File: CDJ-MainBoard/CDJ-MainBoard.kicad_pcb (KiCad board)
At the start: 4 copper layers, 304.6 x 160 mm, 160 parts, among them J1 J_FAN_PWM, J10 USB_DJ_STICK (USB3_A), J11 USB_SCREEN (USB3_A), J12 HR911130A, J13 PI HDMI_0 (HDMI_D_1.4 micro), J14 PI HDMI_0 (HDMI_D_1.4 micro), J15 USB_C_Receptacle_USB2.0_16P, J16 J_JOG, J17 J_PLAY, J18 J_ENCODER_BACK, J19 J_TOUCH, J2 PJ-611E 6.35mm jack, J20 J_LOOP, J21 J_MASTER_TEMPO, J22 J_TEMPO, J3 J_RCA_L (white), J4 J_RCA_R (red), J5 PJ-320D 3.5mm jack, J6 J_ISP_ATMEGA, J7 J_I2C, J8 AUX POWER USB_A, J9 USB_C_Receptacle_USB2.0_16P, SW1 DSWB05LHGET, SW2 PWR_BUT_CM5, SW3 SW_MAIN_POWER, SW4 RESET_BTN, U1 Compute_Module_5_Functional, U10 AP2112K-3.3 DIGITAL PSU LDO, U11 AP2112K-3.3 ANALOG AUDIO LDO, U12 CH224K, U13 SY8368AQQC, U14 ATmega32U4-A (Arduino MIDI co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, U2 PCM5122PW, U3 AP2553W6-7, U4 AP2553W6-7, U5 AP2553W6-7, U6 USBLC6-2SC6, U7 USBLC6-2SC6, U8 USBLC6-2SC6, U9 AP2553W6-7, X1 X322516MLB4SI

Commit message: Route the buck and fixed pinout on ethernet and 3D model offsets
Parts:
- removed J22: J_TEMPO, Connector_JST:JST_PH_B5B-PH-K_1x05_P2.00mm_Vertical
- added C60: 10uF, PCM_JLCPCB:C_0805, F.Cu at (19.3, 44.2)
- added C61: 100nF, PCM_JLCPCB:C_0402, F.Cu at (173.0, 97.5)
- added C62: 100nF, PCM_JLCPCB:C_0402, F.Cu at (173.0, 99.3)
- added C63: 100nF, PCM_JLCPCB:C_0402, F.Cu at (173.0, 101.2)
- added R41: 10kΩ, PCM_JLCPCB:R_0402, F.Cu at (85.5, 125.5)
- added R52: 10kΩ, PCM_JLCPCB:R_0402, F.Cu at (134.0, 131.9)
- added R53: 4.7kΩ, PCM_JLCPCB:R_0402, F.Cu at (188.5, 127.9)
- added R54: 4.7kΩ, PCM_JLCPCB:R_0402, F.Cu at (188.5, 129.4)
- added R55: 10kΩ, PCM_JLCPCB:R_0402, F.Cu at (168.5, 140.5)
- added R56: 330Ω, PCM_JLCPCB:R_0402, F.Cu at (168.5, 138.7)
- added R57: 330Ω, PCM_JLCPCB:R_0402, F.Cu at (168.5, 136.8)
- added R58: 330Ω, PCM_JLCPCB:R_0402, F.Cu at (168.5, 135.0)
- added R59: 330Ω, PCM_JLCPCB:R_0402, F.Cu at (168.5, 133.1)
- added R60: 330Ω, PCM_JLCPCB:R_0402, F.Cu at (168.5, 131.3)
- added R61: 330Ω, PCM_JLCPCB:R_0402, F.Cu at (168.5, 129.4)
- added R62: 330Ω, PCM_JLCPCB:R_0402, F.Cu at (188.5, 142.0)
- added R63: 330Ω, PCM_JLCPCB:R_0402, F.Cu at (188.5, 140.1)
- added R64: 330Ω, PCM_JLCPCB:R_0402, F.Cu at (188.5, 138.3)
- added R65: 330Ω, PCM_JLCPCB:R_0402, F.Cu at (188.5, 136.4)
- added R66: 330Ω, PCM_JLCPCB:R_0402, F.Cu at (188.5, 134.6)
- added R67: 330Ω, PCM_JLCPCB:R_0402, F.Cu at (188.5, 132.7)
- added R68: 330Ω, PCM_JLCPCB:R_0402, F.Cu at (188.5, 130.9)
- added TP12: PF7, TestPoint:TestPoint_Pad_2.0x2.0mm, F.Cu at (66.4, 104.5)
- added TP13: PF6, TestPoint:TestPoint_Pad_2.0x2.0mm, F.Cu at (66.4, 108.5)
- added TP14: PF5, TestPoint:TestPoint_Pad_2.0x2.0mm, F.Cu at (70.5, 104.5)
- added TP15: PF4, TestPoint:TestPoint_Pad_2.0x2.0mm, F.Cu at (70.5, 108.5)
- added TP16: PF1, TestPoint:TestPoint_Pad_2.0x2.0mm, F.Cu at (74.5, 104.5)
- added TP18: PC7, TestPoint:TestPoint_Pad_2.0x2.0mm, F.Cu at (74.5, 108.5)
- added TP24: I2C_SDA_ARDUINO, TestPoint:TestPoint_Pad_1.5x1.5mm, F.Cu at (80.5, 104.5)
- added TP25: I2C_SCL_ARDUINO, TestPoint:TestPoint_Pad_1.5x1.5mm, F.Cu at (80.5, 109.5)
- added U16: 74HC4067PW,118, JLC2KiCad_lib-footprints:TSSOP-28_L9.8-W6.6-P0.65-BL, F.Cu at (118.0, 133.0)
- added U17: PCM5122PW, Package_SO:TSSOP-28_4.4x9.7mm_P0.65mm, F.Cu at (160.6, -34.7)
- added U18: MCP23017T-E/SS, JLC2KiCad_lib-footprints:SSOP-28_L10.2-W5.3-P0.65-LS7.8-BL, F.Cu at (141.0, 134.5)
- added U19: MCP23017T-E/SS, JLC2KiCad_lib-footprints:SSOP-28_L10.2-W5.3-P0.65-LS7.8-BL, F.Cu at (178.5, 135.6)
- J12: footprint JLC2KiCad_lib-footprints:RJ45-TH_HR911130A -> JLC2KiCad_lib-footprints:RJ45-TH_HR911105A
- J15: value USB_C_Receptacle_USB2.0_16P -> TYPE-C-31-M-12; footprint JLC2KiCad_lib-footprints:USB-C-SMD_TYPE-C-6PIN-2MD-073 -> JLC2KiCad_lib-footprints:USB-C_SMD-TYPE-C-31-M-12_1
- J16: value J_JOG -> J_JOGWHEEL; footprint Connector_JST:JST_PH_B4B-PH-K_1x04_P2.00mm_Vertical -> Connector_JST:JST_PH_B5B-PH-K_1x05_P2.00mm_Vertical
- J17: value J_PLAY -> J_HOTCUES; footprint Connector_JST:JST_PH_B6B-PH-K_1x06_P2.00mm_Vertical -> Connector_JST:JST_PH_B8B-PH-K_1x08_P2.00mm_Vertical
- J18: value J_ENCODER_BACK -> J_LEFT_CTRLS; footprint Connector_JST:JST_PH_B7B-PH-K_1x07_P2.00mm_Vertical -> Connector_JST:JST_PH_B10B-PH-K_1x10_P2.00mm_Vertical
- J19: value J_TOUCH -> J_RIGHT_CTRLS; footprint Connector_JST:JST_PH_B2B-PH-K_1x02_P2.00mm_Vertical -> Connector_JST:JST_PH_B12B-PH-K_1x12_P2.00mm_Vertical
- J20: value J_LOOP -> J_TOP_LEFT; footprint Connector_JST:JST_PH_B8B-PH-K_1x08_P2.00mm_Vertical -> Connector_JST:JST_PH_B10B-PH-K_1x10_P2.00mm_Vertical
- J21: value J_MASTER_TEMPO -> J_TOP_RIGHT; footprint Connector_JST:JST_PH_B4B-PH-K_1x04_P2.00mm_Vertical -> Connector_JST:JST_PH_B8B-PH-K_1x08_P2.00mm_Vertical
- J9: value USB_C_Receptacle_USB2.0_16P -> TYPE-C_16PIN_2MD(073)
- moved J16 157.0 mm to (211.0, 159.0)
- moved TP8 143.9 mm to (116.0, 204.4)
- moved TP9 143.9 mm to (120.0, 209.4)
- moved J18 142.0 mm to (181.0, 158.5)
- moved TP6 120.1 mm to (128.0, 175.9)
- moved J7 111.8 mm to (164.0, 91.0), turned to 90 degrees
- moved J17 105.8 mm to (162.0, 158.5)
- moved J20 100.1 mm to (136.5, 158.0)
- moved TP1 64.4 mm to (220.0, 15.5)
- moved J21 62.4 mm to (116.5, 158.0)
- moved J6 61.8 mm to (81.5, 159.0), turned to 180 degrees
- moved R7 55.2 mm to (171.6, 87.0)
- moved C1 54.5 mm to (185.0, 107.0)
- moved J11 50.5 mm to (194.7, 14.5), turned to 90 degrees
- moved TP5 50.2 mm to (228.8, 38.2)
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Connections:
- C58 pad 1: /Arduino MIDI/BTN_TOUCH -> /Arduino MIDI/JOG_TOUCH
- J15 pad 1: (no net) -> GND
- J15 pad 2: (no net) -> GND
- J15 pad 3: (no net) -> GND
- J15 pad 4: (no net) -> GND
- J16 pad 1: /Arduino MIDI/JOG2 -> /Arduino MIDI/JOG1
- J16 pad 2: /Arduino MIDI/JOG1 -> ISP_SCK
- J16 pad 3: +5V -> /Arduino MIDI/JOG_TOUCH
- J16 pad 4: GND -> +5V
- J17 pad 1: GND -> /Arduino MIDI/BTN_HOTCUE_1
- J17 pad 2: ISP_SCK -> /Arduino MIDI/BTN_HOTCUE_2
- J17 pad 3: ISP_MOSI -> /Arduino MIDI/BTN_HOTCUE_3
- J17 pad 4: ISP_MISO -> /Arduino MIDI/LED_HOTCUE1
- J17 pad 5: /Arduino MIDI/LED_CUE -> /Arduino MIDI/LED_HOTCUE2
- J17 pad 6: +5V -> /Arduino MIDI/LED_HOTCUE3
- J18 pad 1: GND -> /Arduino MIDI/BTN_PLAY
- J18 pad 2: /Arduino MIDI/ENC_A -> /Arduino MIDI/BTN_CUE
- J18 pad 3: /Arduino MIDI/ENC_B -> /Arduino MIDI/BTN_SEARCH_L
- J18 pad 4: /Arduino MIDI/ENC_SW -> /Arduino MIDI/BTN_SEARCH_R
- J18 pad 5: /Arduino MIDI/BTN_BACK -> /Arduino MIDI/BTN_TRACK_L
- J18 pad 6: /Arduino MIDI/LED_BACK -> /Arduino MIDI/BTN_TRACK_R
- J18 pad 7: +5V -> /Arduino MIDI/LED_PLAY
- J19 pad 1: /Arduino MIDI/BTN_TOUCH -> /Arduino MIDI/BTN_TEMPO_RST
- J19 pad 2: GND -> /Arduino MIDI/BTN_MTEMPO
- J20 pad 1: GND -> /Arduino MIDI/BTN_DIRECTION
- J20 pad 5: /Arduino MIDI/LED_LOOP_IN -> /Arduino MIDI/LED_DIRECTION
- J20 pad 6: /Arduino MIDI/LED_LOOP_OUT -> /Arduino MIDI/LED_LOOP_IN
- J20 pad 7: /Arduino MIDI/LED_RELOOP -> /Arduino MIDI/LED_LOOP_OUT
- J20 pad 8: +5V -> /Arduino MIDI/LED_RELOOP
- J21 pad 1: GND -> /Arduino MIDI/BTN_BACK
- J21 pad 2: /Arduino MIDI/BTN_MTEMPO -> /Arduino MIDI/TRACK_ENC_A
- J21 pad 3: /Arduino MIDI/LED_MTEMPO -> /Arduino MIDI/TRACK_ENC_B
- J21 pad 4: +5V -> /Arduino MIDI/TRACK_ENC_PUSH
- J9 pad 1: (no net) -> GND
- J9 pad 10: (no net) -> Net-(J9-CC2)
- J9 pad 11: (no net) -> /USB DJ Ports/USB_C_DJ_VBUS
- J9 pad 12: (no net) -> GND
- J9 pad 13: (no net) -> GND
- J9 pad 14: (no net) -> GND
- J9 pad 2: (no net) -> /USB DJ Ports/USB_C_DJ_VBUS
- J9 pad 3: (no net) -> unconnected-(J9-SBU2-Pad3)
- J9 pad 4: (no net) -> Net-(J9-CC1)
- J9 pad 5: (no net) -> Net-(J9-DN1)
- J9 pad 6: (no net) -> Net-(J9-DP1)
- J9 pad 7: (no net) -> Net-(J9-DN1)
- J9 pad 8: (no net) -> Net-(J9-DP1)
- J9 pad 9: (no net) -> unconnected-(J9-SBU1-Pad9)
- R37 pad 2: /Arduino MIDI/BTN_TOUCH -> /Arduino MIDI/JOG_TOUCH
- SW1 pad 1: /S_WIFI_UP -> /Compute Module/S_WIFI_GND
- SW1 pad 2: /S_BT_UP -> /Compute Module/S_BT_GND
- SW1 pad 3: /S_BOOT_UP -> /Compute Module/S_BOOT_GND
- SW1 pad 4: /S_EEPROM_WP_UP -> /Compute Module/S_EEPROM_WP_GND
- U1 pad 20: /S_EEPROM_WP_GND -> /Compute Module/S_EEPROM_WP_GND
- U1 pad 89: /S_WIFI_GND -> /Compute Module/S_WIFI_GND
- U1 pad 91: /S_BT_GND -> /Compute Module/S_BT_GND
- U1 pad 93: /S_BOOT_GND -> /Compute Module/S_BOOT_GND
- U12 pad 4: Net-(U12-DP) -> Net-(J15-DP1)
- U12 pad 5: Net-(U12-DM) -> Net-(J15-DN1)
- U14 pad 1: /Arduino MIDI/LED_TEMPO_RST -> /Arduino MIDI/JOG_TOUCH
- U14 pad 12: /Arduino MIDI/BTN_RELOOP -> /Arduino MIDI/TRACK_ENC_PUSH
- U14 pad 18: /Arduino MIDI/JOG2 -> /Arduino MIDI/I2C_SCL_ATMEGA
- U14 pad 19: /Arduino MIDI/JOG1 -> /Arduino MIDI/I2C_SDA_ATMEGA
- U14 pad 22: /Arduino MIDI/BTN_TOUCH -> /Arduino MIDI/MUX_S3
- U14 pad 25: /Arduino MIDI/BTN_MTEMPO -> /Arduino MIDI/MUX_S0
- U14 pad 26: /Arduino MIDI/LED_RELOOP -> /Arduino MIDI/MUX_S1
- U14 pad 27: /Arduino MIDI/LED_MTEMPO -> /Arduino MIDI/MUX_S2
- U14 pad 28: /Arduino MIDI/LED_CUE -> /Arduino MIDI/MCP1_INT
- U14 pad 29: /Arduino MIDI/BTN_LOOP_IN -> /Arduino MIDI/MCP2_INT
- U14 pad 30: /Arduino MIDI/BTN_LOOP_OUT -> /Arduino MIDI/TRACK_ENC_A
- U14 pad 31: /Arduino MIDI/LED_LOOP_IN -> /Arduino MIDI/TRACK_ENC_B
- U14 pad 32: /Arduino MIDI/LED_LOOP_OUT -> Net-(U14-PC7)
- U14 pad 33: /Arduino MIDI/BTN_TEMPO_RST -> Net-(U14-~{HWB}/PE2)
- U14 pad 36: /Arduino MIDI/LED_BACK -> Net-(U14-PF7)
- U14 pad 37: /Arduino MIDI/BTN_BACK -> Net-(U14-PF6)
- U14 pad 38: /Arduino MIDI/ENC_SW -> Net-(U14-PF5)
- U14 pad 39: /Arduino MIDI/ENC_B -> Net-(U14-PF4)
- U14 pad 40: /Arduino MIDI/ENC_A -> Net-(U14-PF1)
- U14 pad 41: /Arduino MIDI/FADER_ADIN -> /Arduino MIDI/MUX_SIG
- U14 pad 8: unconnected-(U14-PB0-Pad8) -> /Arduino MIDI/JOG1
- U6 pad 1: Net-(J9-D--PadA7) -> Net-(J9-DN1)
- U6 pad 3: Net-(J9-D+-PadA6) -> Net-(J9-DP1)
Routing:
- net +20V_USB: track 0.00 -> 34.1 mm
- net GND: track 0.00 -> 20.9 mm, vias 0 -> 43
- net +5V: track 0.00 -> 20.0 mm, vias 0 -> 17
- net +20V_USB_RAIL: track 0.00 -> 17.8 mm, vias 0 -> 2
- net Net-(J15-CC2): track 0.00 -> 16.1 mm, vias 0 -> 2
- net Net-(U12-VBUS): track 0.00 -> 14.7 mm, vias 0 -> 1
- net Net-(J15-CC1): track 0.00 -> 13.9 mm
- net Net-(J15-DN1): track 0.00 -> 13.2 mm
- net Net-(J15-DP1): track 0.00 -> 12.3 mm
- net Net-(U13-LX): track 0.00 -> 10.1 mm, vias 0 -> 3
- net Net-(U12-VDD): track 0.00 -> 8.41 mm
- net +3.3V: track 0.00 -> 5.75 mm
- net Net-(U13-EN): track 0.00 -> 4.97 mm
- net Net-(U13-FB): track 0.00 -> 4.83 mm
- net +3.3V_ANALOG: track 0.00 -> 4.78 mm
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- added copper zone on In1.Cu, net +5V
- added copper zone on B.Cu, net GND
- added copper zone on In1.Cu, net GND
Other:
- board size 304.6 x 160 mm -> 250 x 160 mm

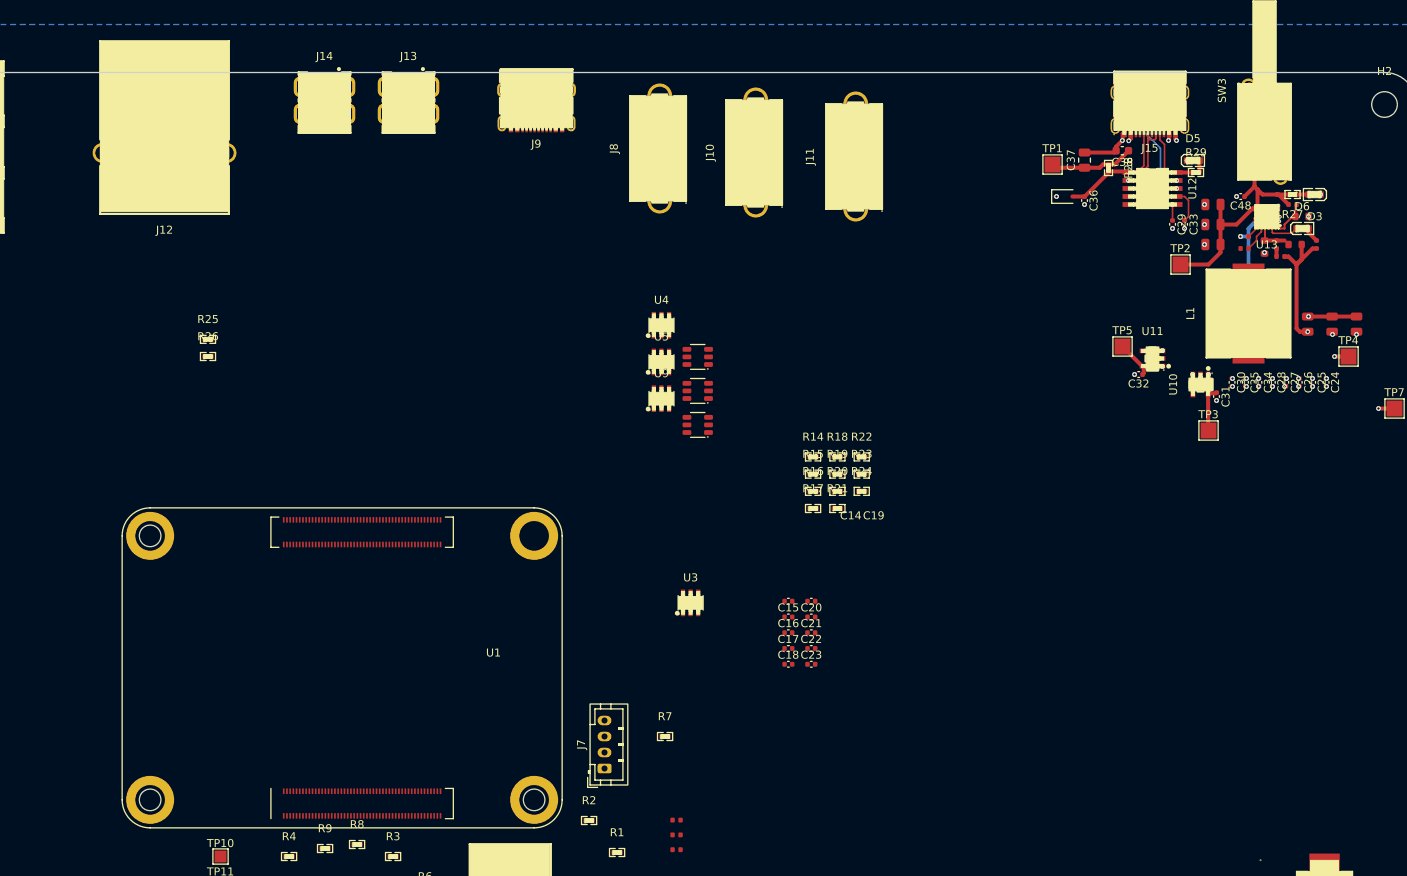
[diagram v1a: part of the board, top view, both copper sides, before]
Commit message: Route the two HDMI ports and remove via-in-pads or tent them
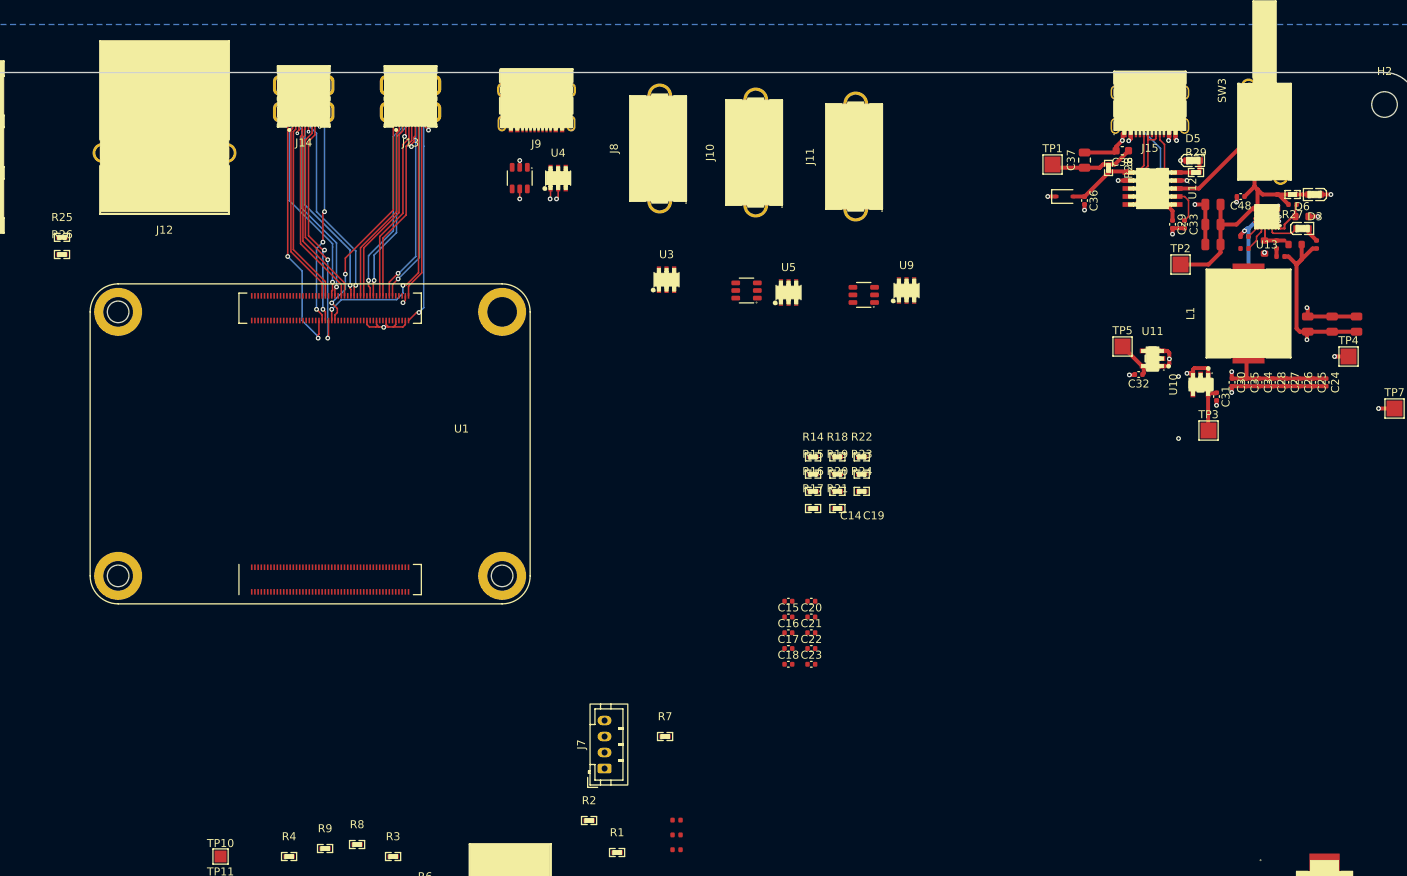
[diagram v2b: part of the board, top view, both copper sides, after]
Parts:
- moved U3 40.5 mm to (171.8, 29.9)
- moved U9 33.5 mm to (201.8, 31.2)
- moved U6 31.5 mm to (153.4, 17.2), turned to 90 degrees
- moved U1 28.3 mm to (129.7, 50.4)
- moved U8 26.4 mm to (196.4, 31.8)
- moved U4 22.5 mm to (158.2, 17.2)
- moved R25 22.3 mm to (96.2, 24.6)
- moved R26 22.3 mm to (96.2, 26.8)
- moved U5 18.1 mm to (187.0, 31.5)
- moved U7 14.0 mm to (181.8, 31.2)
- moved J14 2.87 mm to (126.4, 7.98), turned to 180 degrees
- moved J13 1.23 mm to (139.8, 7.98), turned to 180 degrees
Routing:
- net GND: track 20.9 -> 81.1 mm, vias 43 -> 47
- net +5V: track 20.0 -> 55.7 mm, vias 17 -> 10
- net Net-(J13-CEC): track 0.00 -> 33.4 mm, vias 0 -> 2
- net Net-(J14-HPD/HEAC-): track 0.00 -> 30.7 mm, vias 0 -> 2
- net Net-(J14-CEC): track 0.00 -> 30.6 mm, vias 0 -> 2
- net Net-(J14-SDA): track 0.00 -> 29.0 mm, vias 0 -> 4
- net Net-(J14-CK+): track 0.00 -> 28.8 mm, vias 0 -> 2
- net Net-(J14-D1+): track 0.00 -> 28.6 mm, vias 0 -> 2
- net Net-(J13-D1-): track 0.00 -> 28.6 mm, vias 0 -> 2
- net Net-(J13-CK+): track 0.00 -> 28.4 mm, vias 0 -> 2
- net Net-(J13-HPD/HEAC-): track 0.00 -> 28.4 mm, vias 0 -> 2
- net Net-(J13-D1+): track 0.00 -> 28.4 mm, vias 0 -> 2
- net Net-(J13-CK-): track 0.00 -> 28.2 mm, vias 0 -> 2
- net Net-(J13-SDA): track 0.00 -> 28.2 mm, vias 0 -> 2
- net Net-(J14-CK-): track 0.00 -> 27.5 mm, vias 0 -> 2
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- added copper zone on In2.Cu, net +5V
- added copper zone on In2.Cu, net GND
- removed copper zone on In1.Cu, net +5V

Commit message: Route the ethernet port
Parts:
- J12: footprint JLC2KiCad_lib-footprints:RJ45-TH_HR911105A -> JLC2KiCad_lib-footprints:RJ45-TH_HR911130A
- moved TP3 148.5 mm to (91.2, 41.6)
- moved U11 147.2 mm to (86.1, 55.0)
- moved C31 146.8 mm to (93.8, 41.1)
- moved TP5 144.9 mm to (86.0, 63.2)
- moved U10 143.5 mm to (95.1, 38.2), turned to 0 degrees
- moved C32 138.1 mm to (94.3, 63.2), turned to 0 degrees
- moved TP8 118.8 mm to (102.2, 86.4)
- moved TP9 118.8 mm to (106.2, 91.4)
- moved TP6 53.3 mm to (143.2, 124.8)
- moved D1 51.1 mm to (134.6, 122.4)
- moved R26 27.3 mm to (118.6, 11.1), turned to -90 degrees
- moved R25 13.8 mm to (98.4, 11.0), turned to -90 degrees
- moved J12 3.10 mm to (108.9, 16.1), turned to 0 degrees
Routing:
- net /HDMI and Ethernet/eth_nled_2: track 0.00 -> 71.5 mm, vias 0 -> 2
- net /HDMI and Ethernet/eth_nled_3: track 0.00 -> 68.2 mm, vias 0 -> 1
- net /HDMI and Ethernet/eth_p3_n: track 0.00 -> 55.2 mm, vias 0 -> 1
- net /HDMI and Ethernet/eth_p3_p: track 0.00 -> 54.7 mm, vias 0 -> 1
- net /HDMI and Ethernet/eth_p2_n: track 0.00 -> 53.9 mm, vias 0 -> 1
- net /HDMI and Ethernet/eth_p2_p: track 0.00 -> 51.3 mm, vias 0 -> 1
- net /HDMI and Ethernet/eth_p1_p: track 0.00 -> 49.3 mm, vias 0 -> 1
- net /HDMI and Ethernet/eth_p0_p: track 0.00 -> 48.9 mm
- net /HDMI and Ethernet/eth_p1_n: track 0.00 -> 48.5 mm
- net /HDMI and Ethernet/eth_p0_n: track 0.00 -> 46.8 mm
- net +3.3V: track 5.75 -> 13.1 mm, vias 0 -> 4
- net +3.3V_ANALOG: track 4.78 -> 0.20 mm
- net Net-(J12-Pad14): track 0.00 -> 4.41 mm
- net Net-(J12-Pad11): track 0.00 -> 3.68 mm
- net +5V: track 55.7 -> 52.6 mm, vias 10 -> 9
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- added copper zone on In2.Cu, net +3.3V

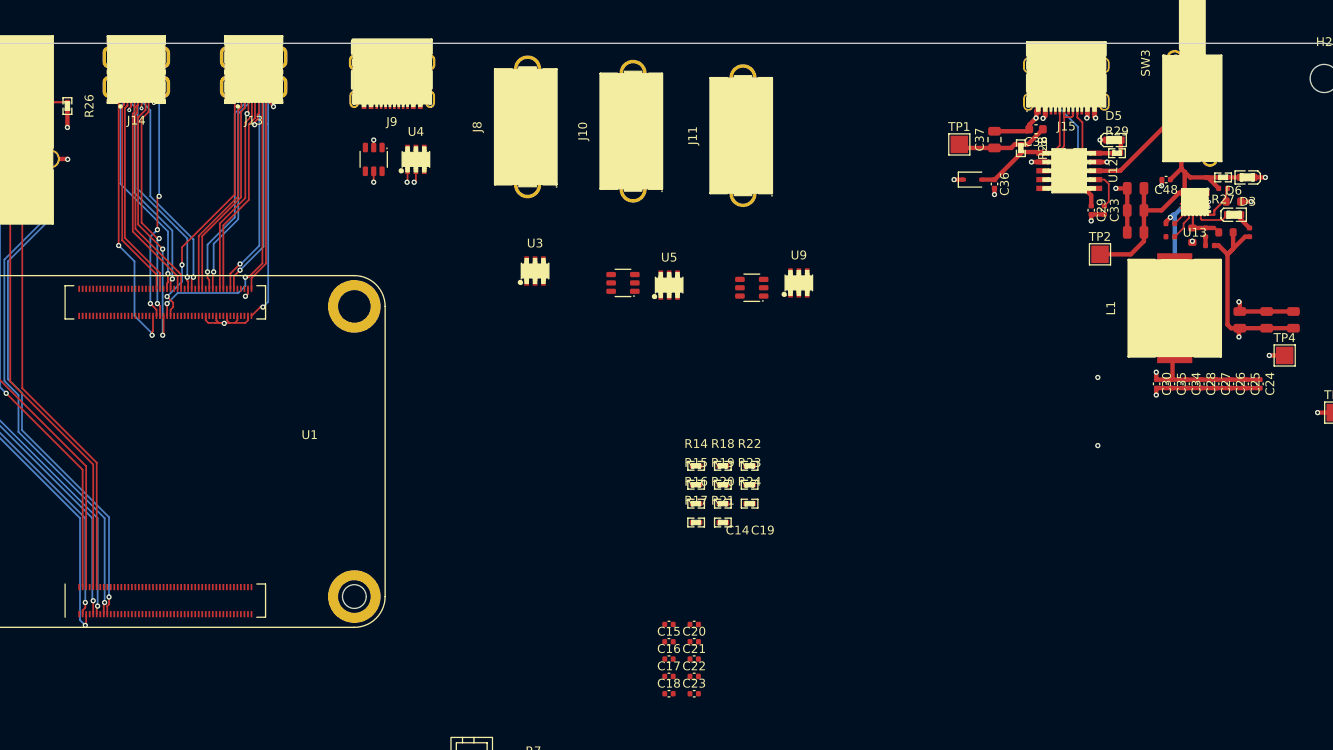
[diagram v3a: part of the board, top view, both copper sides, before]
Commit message: Route all 4 USB ports
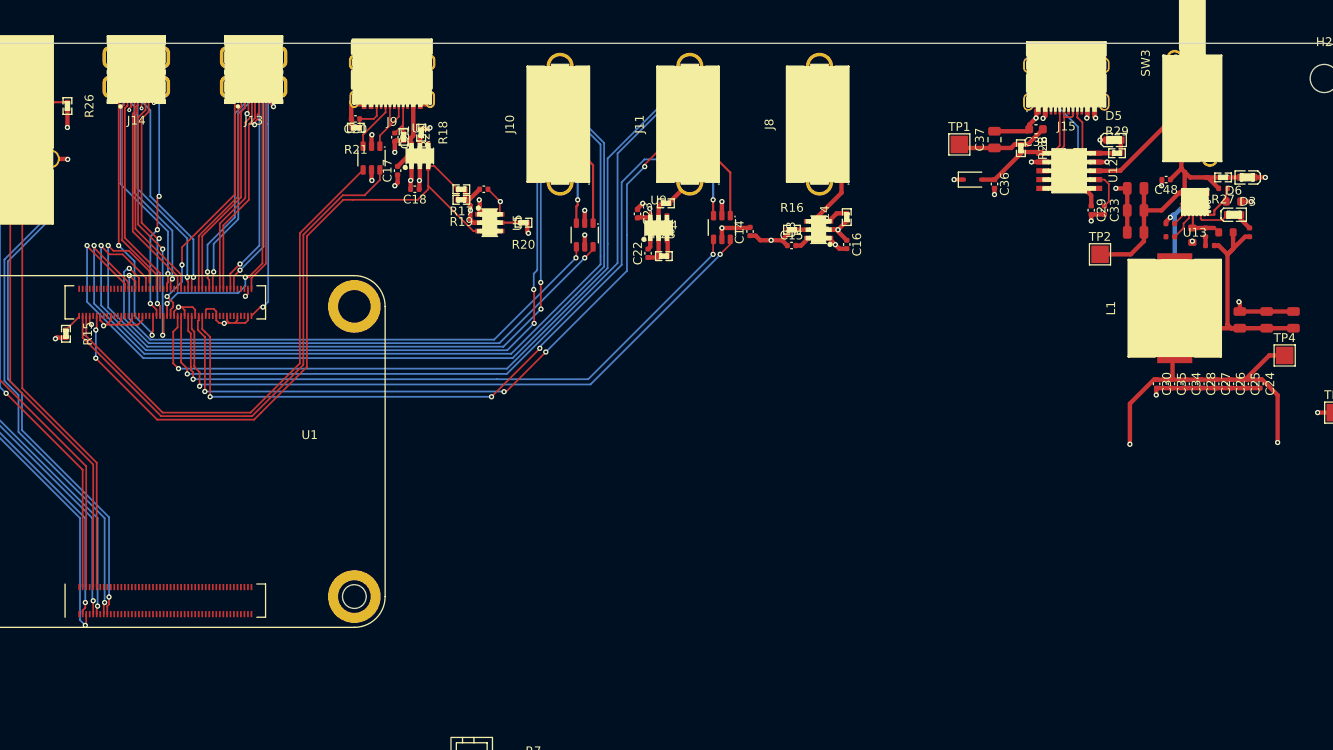
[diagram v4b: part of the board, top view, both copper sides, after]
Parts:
- moved R15 73.7 mm to (118.4, 37.0), turned to -90 degrees
- moved C20 70.9 mm to (151.3, 12.6), turned to 180 degrees
- moved C21 68.4 mm to (155.8, 14.7), turned to -90 degrees
- moved C17 65.3 mm to (156.1, 18.5), turned to 90 degrees
- moved C18 64.2 mm to (158.1, 20.6), turned to 180 degrees
- moved R21 61.3 mm to (151.4, 13.6), turned to 180 degrees
- moved C19 55.0 mm to (165.9, 20.6)
- moved C23 54.9 mm to (183.4, 23.4), turned to -90 degrees
- moved R22 54.3 mm to (156.8, 14.6), turned to -90 degrees
- moved C16 51.3 mm to (207.2, 26.9), turned to -90 degrees
- moved R18 51.1 mm to (158.8, 14.2), turned to -90 degrees
- moved C22 48.4 mm to (184.6, 27.9), turned to 90 degrees
- moved C15 47.2 mm to (200.9, 27.0)
- moved R17 46.4 mm to (163.4, 20.6), turned to 180 degrees
- moved C14 45.6 mm to (196.2, 25.4), turned to 90 degrees
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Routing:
- net /USB DJ Ports/USB_DJ_SSRXM: track 0.00 -> 102.4 mm, vias 0 -> 1
- net /USB DJ Ports/USB_DJ_SSRXP: track 0.00 -> 98.8 mm, vias 0 -> 1
- net /USB DJ Ports/USB_DJ_SSTXM: track 0.00 -> 88.7 mm, vias 0 -> 3
- net /USB DJ Ports/USB_DJ_SSTXP: track 0.00 -> 84.5 mm, vias 0 -> 3
- net /USB DJ Ports/USB_SCR_SSRXM: track 0.00 -> 83.6 mm, vias 0 -> 1
- net /USB DJ Ports/USB_SCR_SSRXP: track 0.00 -> 82.5 mm, vias 0 -> 1
- net /USB DJ Ports/USB_DJ_VBUS_EN: track 0.00 -> 81.4 mm, vias 0 -> 2
- net /USB DJ Ports/USB_SCR_SSTXM: track 0.00 -> 80.4 mm, vias 0 -> 4
- net /USB DJ Ports/USB_SCR_SSTXP: track 0.00 -> 79.4 mm, vias 0 -> 3
- net /USB DJ Ports/USB_SCR_DM: track 0.00 -> 76.1 mm, vias 0 -> 2
- net /USB DJ Ports/USB_SCR_DP: track 0.00 -> 74.2 mm, vias 0 -> 2
- net /USB DJ Ports/USB_DJ_DM: track 0.00 -> 68.1 mm, vias 0 -> 2
- net /USB DJ Ports/USB_DJ_DP: track 0.00 -> 63.6 mm, vias 0 -> 2
- net GND: track 83.7 -> 146.0 mm, vias 47 -> 62
- net /USB DJ Ports/USB_C_DJ_DM: track 0.00 -> 60.9 mm
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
